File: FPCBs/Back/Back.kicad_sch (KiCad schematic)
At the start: 24 parts, among them J1 To PCB, J2 To Front, J3 Front, J4 EVF_SENSOR, J5 From LCD, SW1 MENU/SET, SW10 -+-, SW11 PLAY, SW12 WHEEL, SW13 S/C/M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

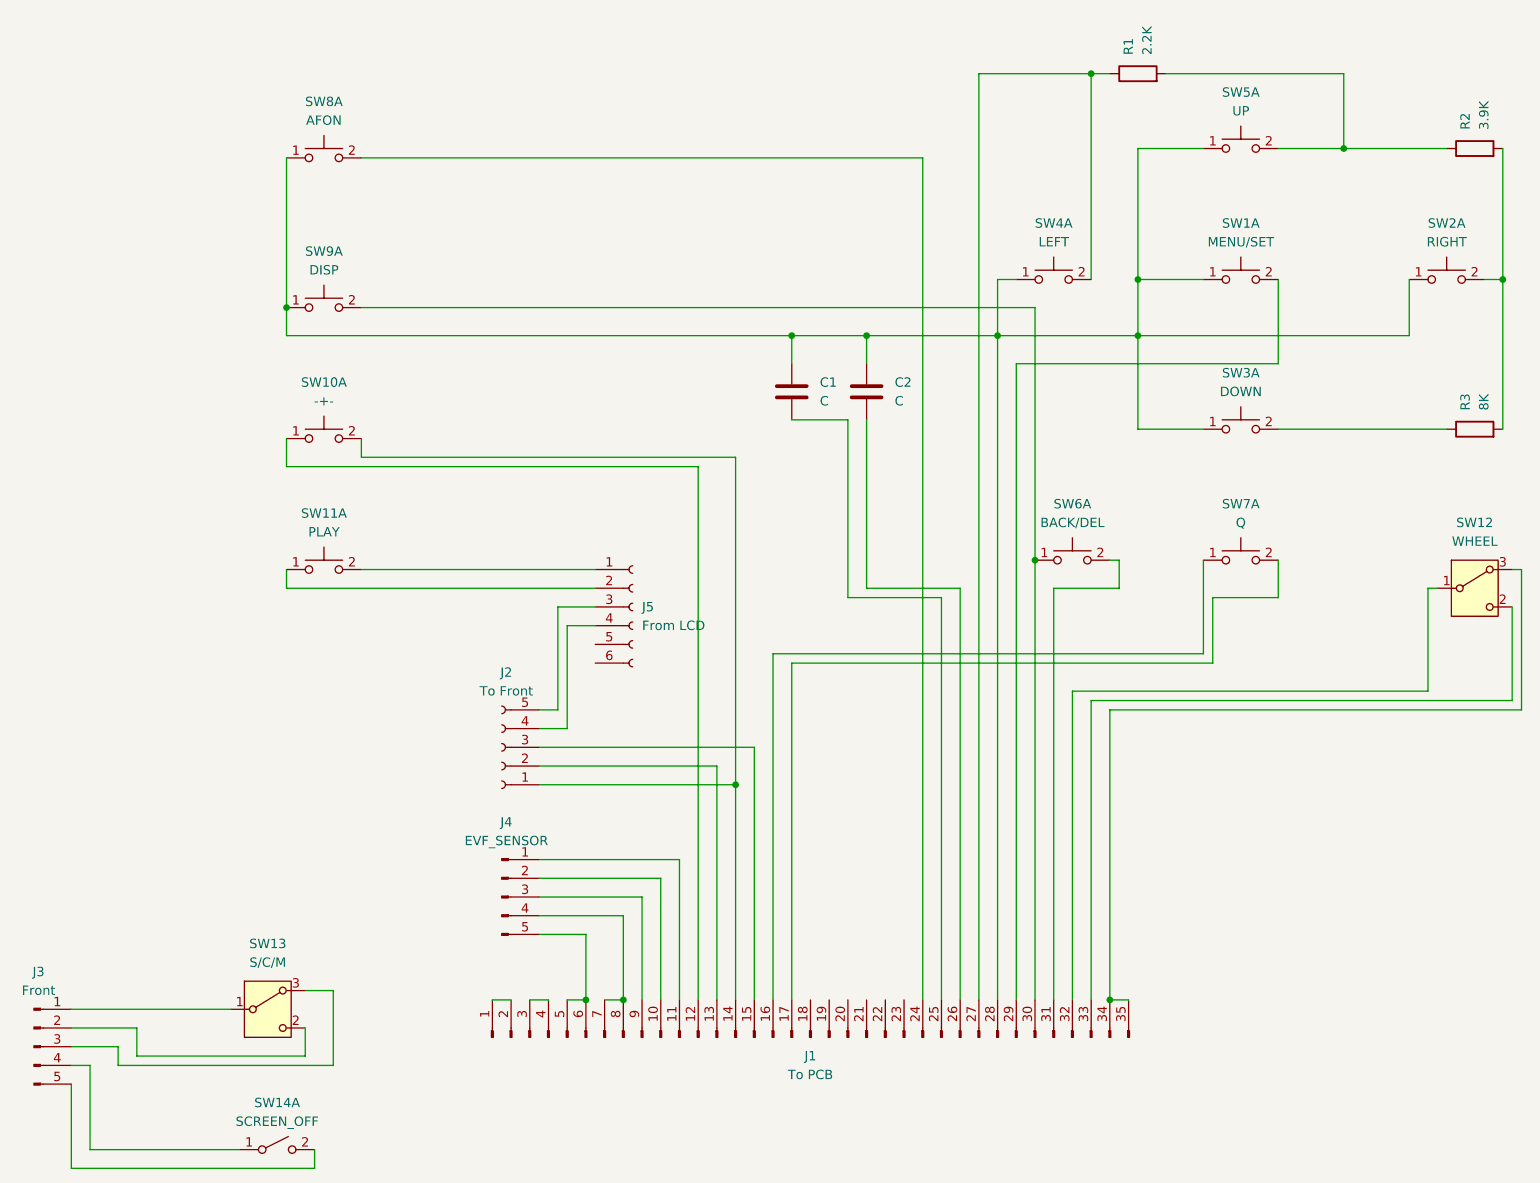
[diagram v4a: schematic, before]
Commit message: Fix back wheel
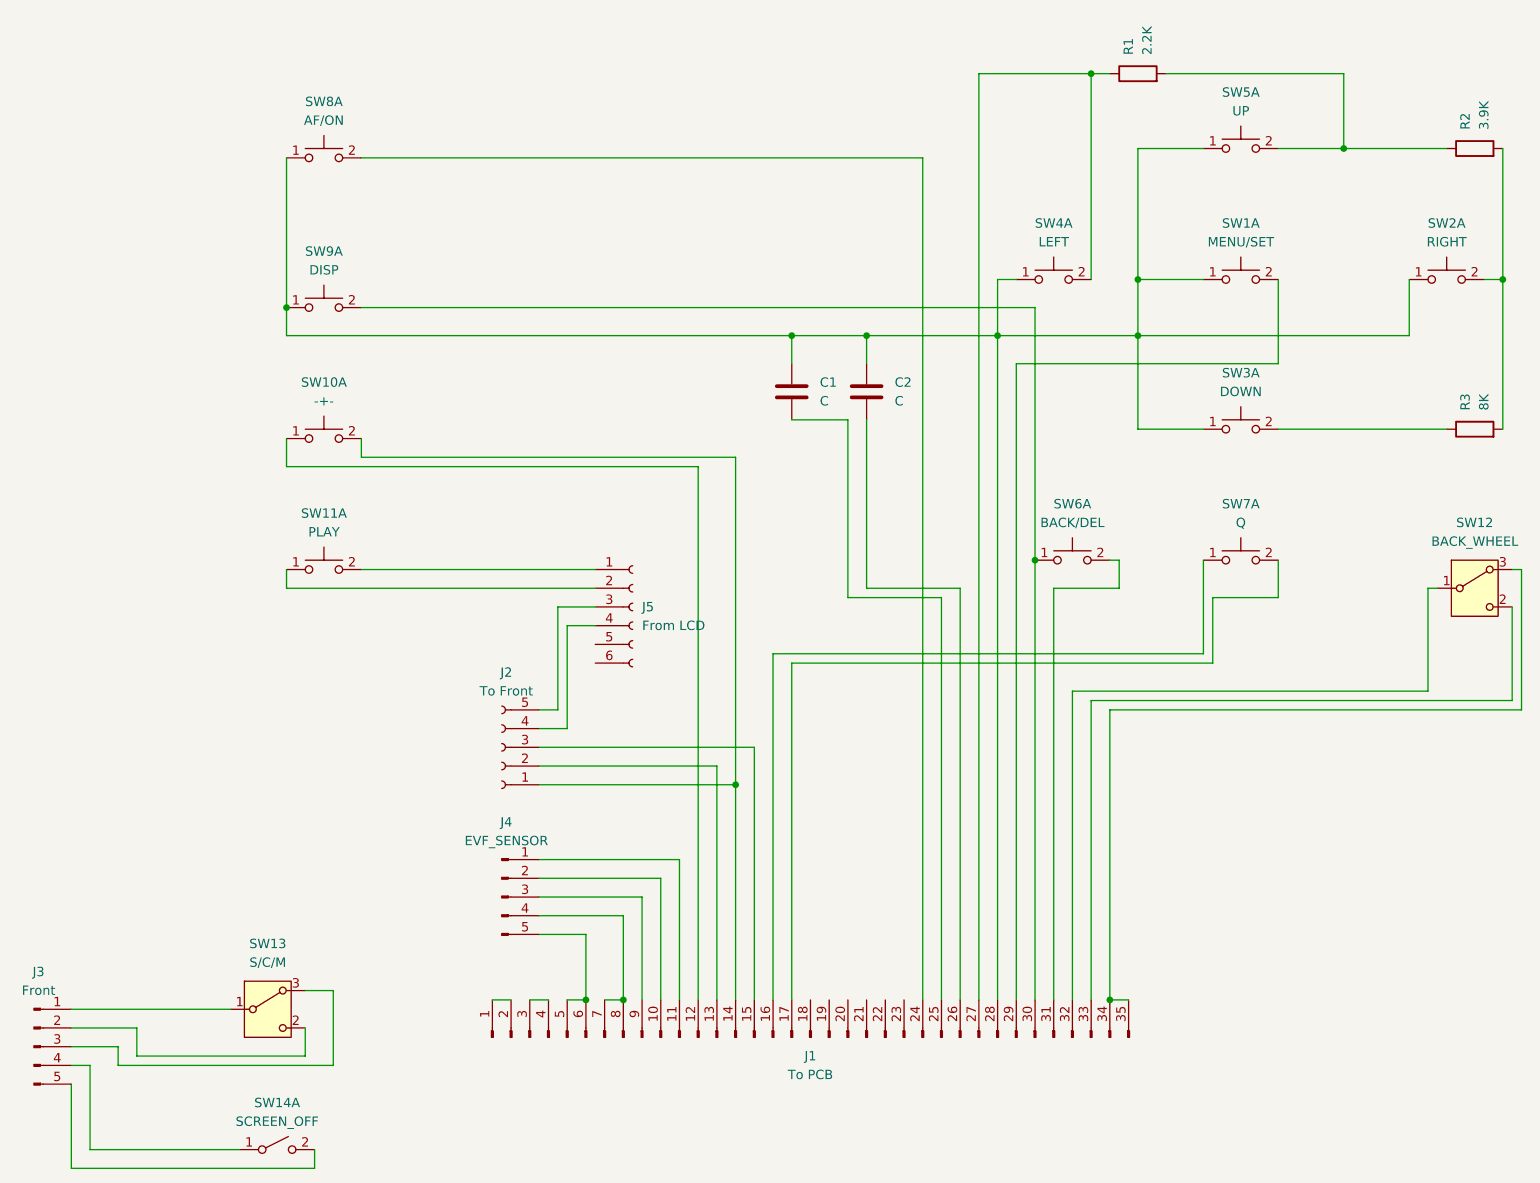
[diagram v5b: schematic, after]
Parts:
- C1, C2, R1, R2, R3: footprint Leica-G9ii:R_2x1mm -> Leica-G9ii:R_0603
- SW12: value WHEEL -> BACK_WHEEL
- SW8: value AFON -> AF/ON
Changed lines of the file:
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@@
 			)
 		)
-		(property "Footprint" "Leica-G9ii:R_2x1mm"
+		(property "Footprint" "Leica-G9ii:R_0603"
 			(at 175.26 28.448 90)
 			(effects
@@
 			)
 		)
-		(property "Footprint" "Leica-G9ii:R_2x1mm"
+		(property "Footprint" "Leica-G9ii:R_0603"
 			(at 139.3952 73.66 0)
 			(effects
@@
 			)
 		)
-		(property "Value" "WHEEL"
+		(property "Value" "BACK_WHEEL"
 			(at 220.98 90.17 0)
 			(effects
@@
 			)
 		)
-		(property "Footprint" "Leica-G9ii:R_2x1mm"
+		(property "Footprint" "Leica-G9ii:R_0603"
 			(at 220.98 38.608 90)
 			(effects
@@
 			)
 		)
-		(property "Value" "AFON"
+		(property "Value" "AF/ON"
 			(at 64.77 33.02 0)
 			(effects
@@
 			)
 		)
-		(property "Footprint" "Leica-G9ii:R_2x1mm"
+		(property "Footprint" "Leica-G9ii:R_0603"
 			(at 129.2352 73.66 0)
 			(effects
@@
 			)
 		)
-		(property "Footprint" "Leica-G9ii:R_2x1mm"
+		(property "Footprint" "Leica-G9ii:R_0603"
 			(at 220.98 76.708 90)
 			(effects
